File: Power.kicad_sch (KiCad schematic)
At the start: 35 parts, among them J1 B2B-PH-SM4-TBLFSN, U4 MCP1727T-3302E/SN, U5 BQ25185DLHR

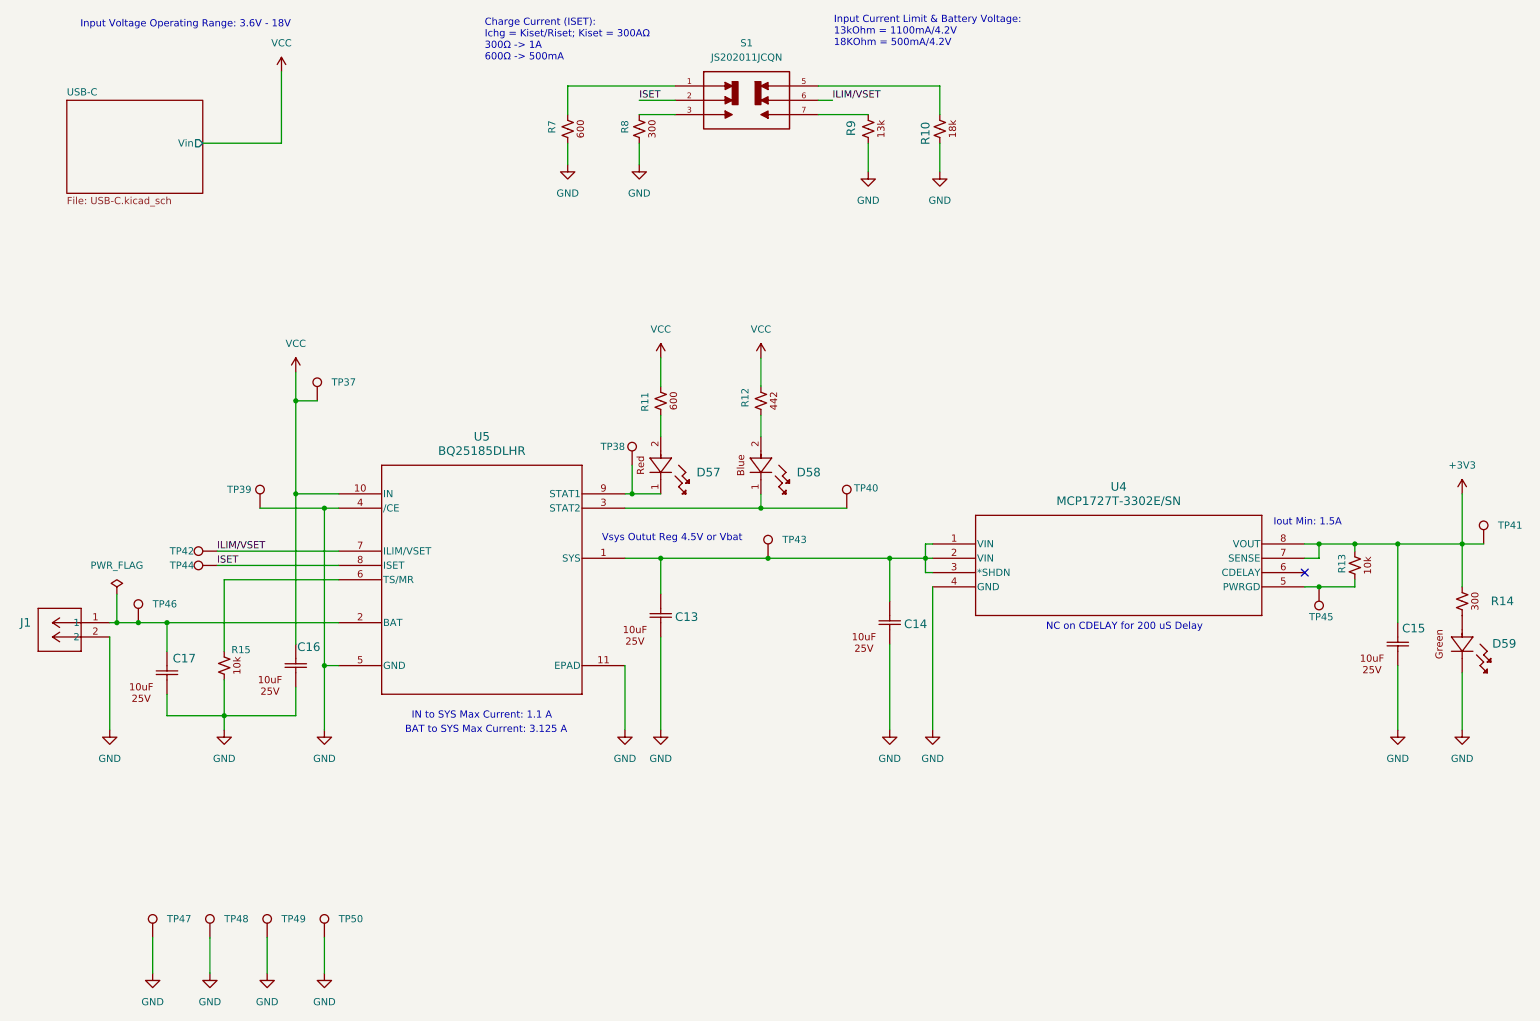
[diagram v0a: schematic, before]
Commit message: Moved all TPs to board area except CS TPs. Deleted some TPs that are less of a priority.
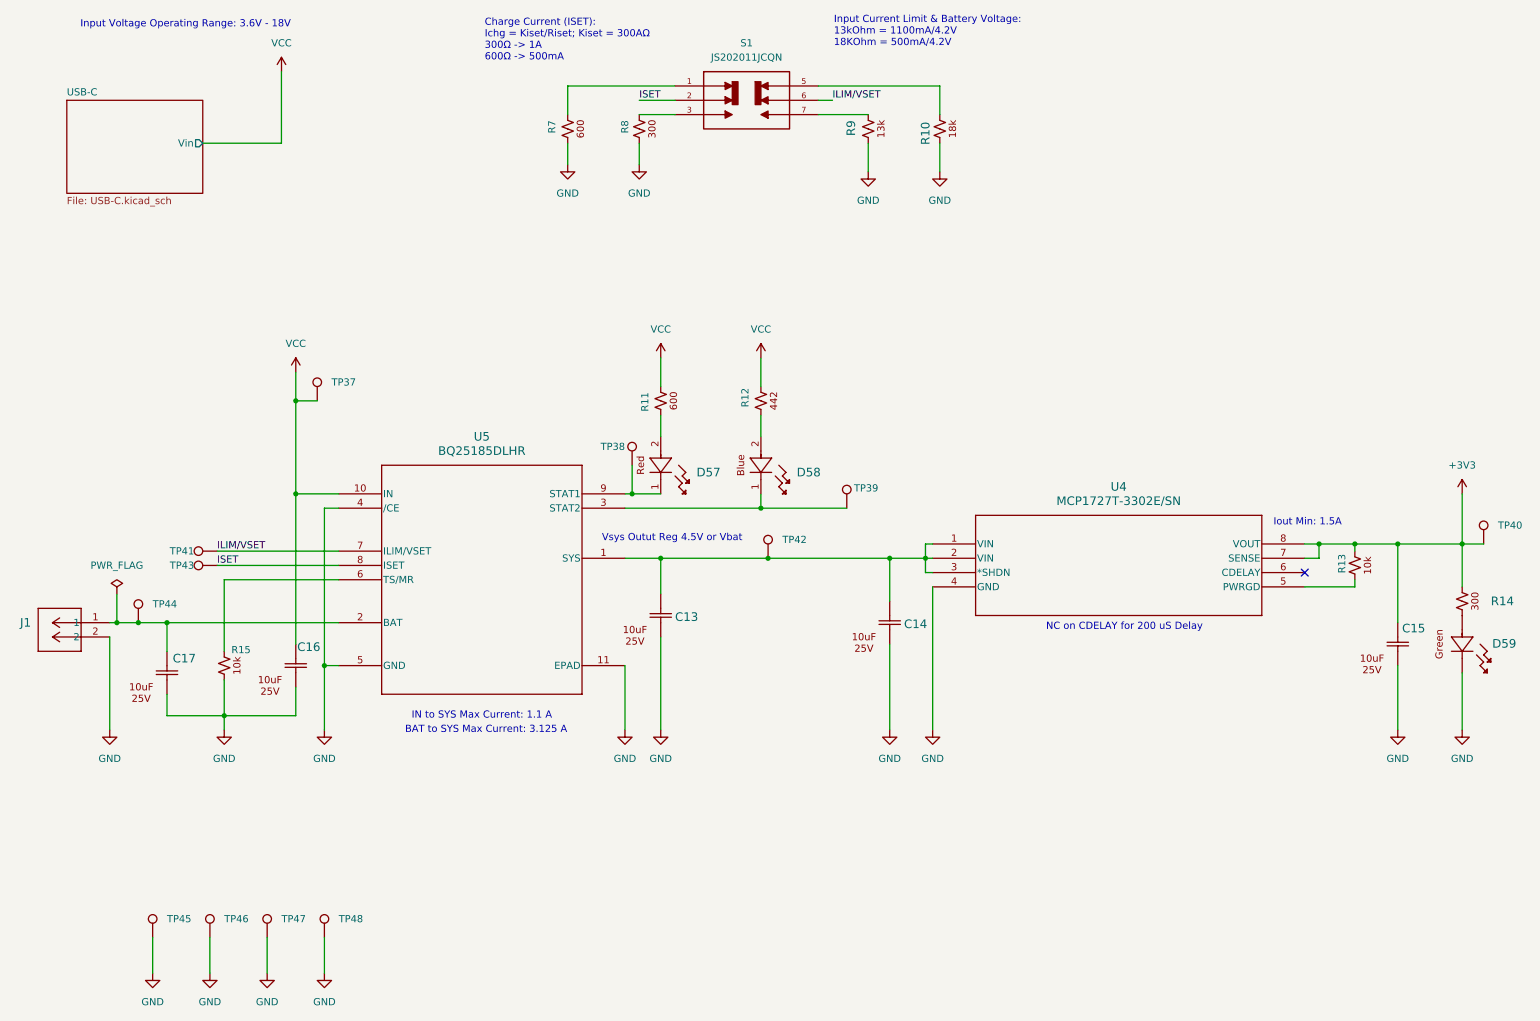
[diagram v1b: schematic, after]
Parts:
- removed TP39, TP45: TestPoint, TestPoint:TestPoint_Pad_D1.0mm, symbol Connector:TestPoint
- renumbered TP40 to TP39, TP41 to TP40, TP42 to TP41, TP43 to TP42, TP44 to TP43, TP46 to TP44, TP47 to TP45, TP48 to TP46, TP49 to TP47, TP50 to TP48
